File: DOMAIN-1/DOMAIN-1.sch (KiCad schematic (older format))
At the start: 245 parts, among them J1 Conn_02x10_Odd_Even, J2 AVR-ISP-6, SW1 SW_Push, U1 AT90USB1286-AU, U2 PRTR5V0U2X, Y1 Crystal_GND24_Small

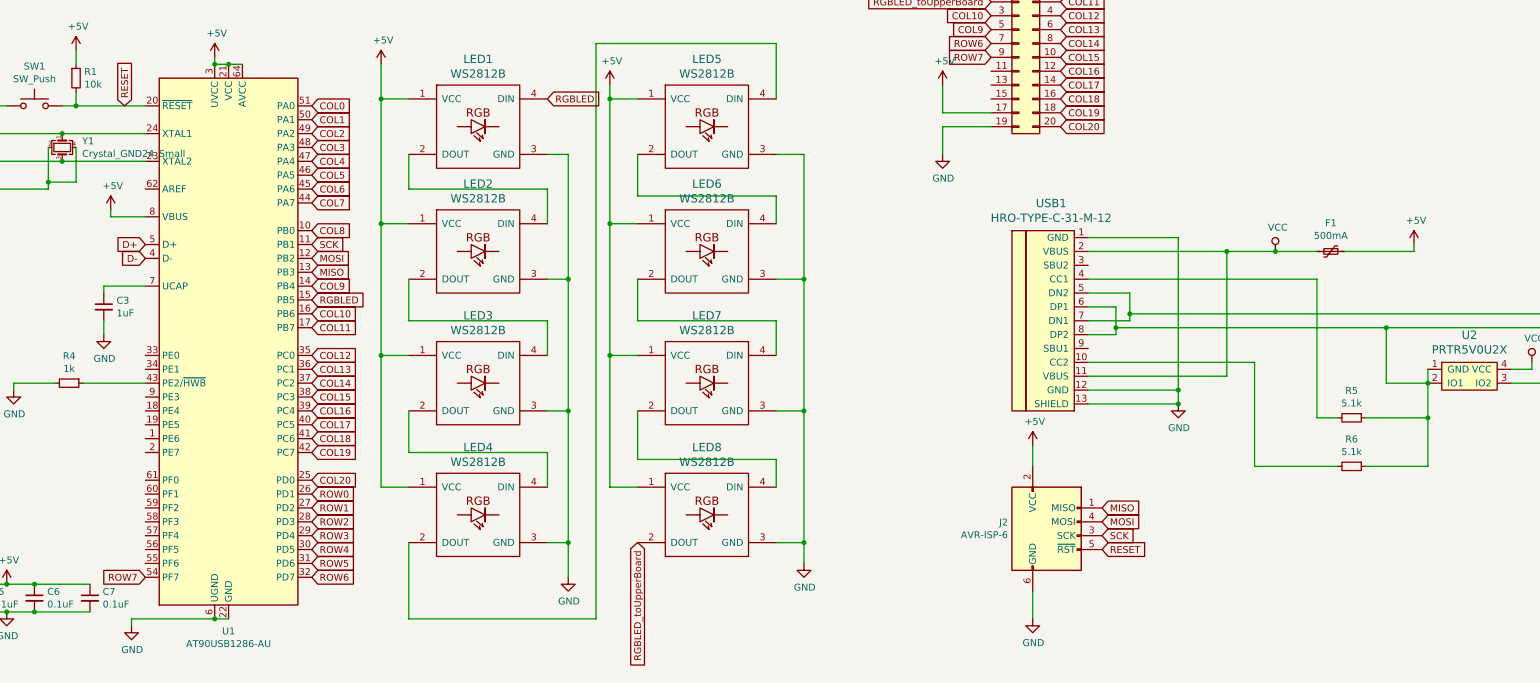
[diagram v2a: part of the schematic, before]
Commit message: Finished LED placement
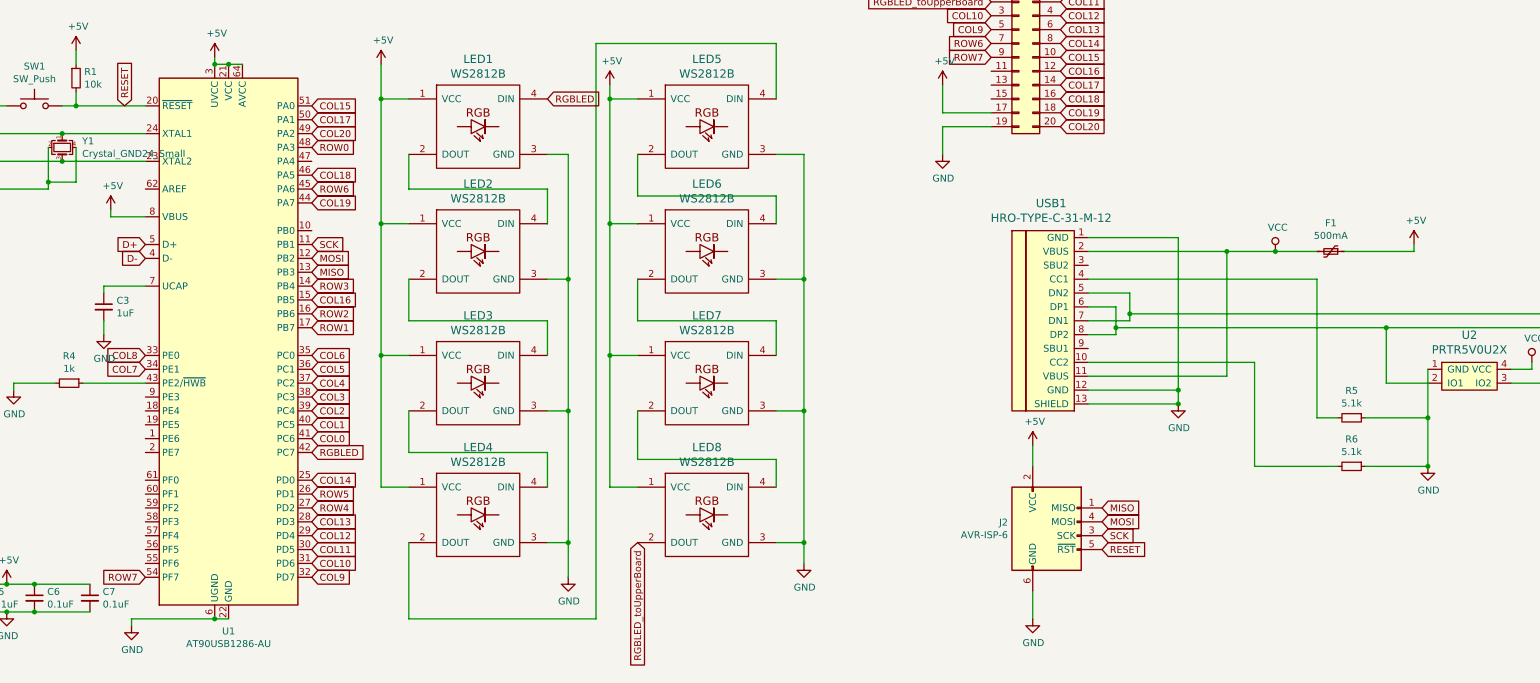
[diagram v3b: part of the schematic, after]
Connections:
- net COL0: now also U1.41 (PC6); no longer U1.51 (PA0)
- net COL1: now also U1.40 (PC5); no longer U1.50 (PA1)
- net COL10: now also U1.31 (PD6); no longer U1.16 (PB6)
- net COL11: now also U1.30 (PD5); no longer U1.17 (PB7)
- net COL12: now also U1.29 (PD4); no longer U1.35 (PC0)
- net COL13: now also U1.28 (PD3); no longer U1.36 (PC1)
- net COL14: now also U1.25 (PD0); no longer U1.37 (PC2)
- net COL15: now also U1.51 (PA0); no longer U1.38 (PC3)
- net COL16: now also U1.15 (PB5); no longer U1.39 (PC4)
- net COL17: now also U1.50 (PA1); no longer U1.40 (PC5)
- net COL18: now also U1.46 (PA5); no longer U1.41 (PC6)
- net COL19: now also U1.44 (PA7); no longer U1.42 (PC7)
- net COL2: now also U1.39 (PC4); no longer U1.49 (PA2)
- net COL20: now also U1.49 (PA2); no longer U1.25 (PD0)
- net COL3: now also U1.38 (PC3); no longer U1.48 (PA3)
- net COL4: now also U1.37 (PC2); no longer U1.47 (PA4)
- net COL5: now also U1.36 (PC1); no longer U1.46 (PA5)
- net COL6: now also U1.35 (PC0); no longer U1.45 (PA6)
- net COL7: now also U1.34 (PE1); no longer U1.44 (PA7)
- net COL8: now also U1.33 (PE0); no longer U1.10 (PB0)
- net COL9: now also U1.32 (PD7); no longer U1.14 (PB4)
- net GND: now also R5.1, R6.1, U2.1 (GND)
- net RGBLED: now also U1.42 (PC7); no longer U1.15 (PB5)
- net ROW0: now also U1.48 (PA3); no longer U1.26 (PD1)
- net ROW1: now also U1.17 (PB7); no longer U1.27 (PD2)
- net ROW2: now also U1.16 (PB6); no longer U1.28 (PD3)
- net ROW3: now also U1.14 (PB4); no longer U1.29 (PD4)
- net ROW4: now also U1.27 (PD2); no longer U1.30 (PD5)
- net ROW5: now also U1.26 (PD1); no longer U1.31 (PD6)
- net ROW6: now also U1.45 (PA6); no longer U1.32 (PD7)
- net at R3.2, U2.2 (IO1), USB1.6 (DP1)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: no longer R5.1, R6.1, U2.1 (GND)
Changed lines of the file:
@@
 Wire Wire Line
 	11500 9750 11050 9750
-Connection ~ 11500 9400
 Wire Wire Line
 	10700 8400 9050 8400
@@
 Wire Wire Line
 	11500 9400 11050 9400
-Wire Wire Line
-	11500 9150 11500 9400
-Connection ~ 11500 9150
-Wire Wire Line
-	11500 9050 11500 9150
 $Comp
 L power:VCC #PWR0103
@@
 Wire Wire Line
 	12100 9150 12350 9150
-$Comp
-L random-keyboard-parts:PRTR5V0U2X U2
-U 1 1 61D145CB
-P 11800 9100
-F 0 "U2" H 11800 9397 60  0000 C CNN
-F 1 "PRTR5V0U2X" H 11800 9291 60  0000 C CNN
-F 2 "random-keyboard-parts:SOT143B" H 11800 9100 60  0001 C CNN
-F 3 "" H 11800 9100 60  0001 C CNN
-	1    11800 9100
-	1    0    0    -1
-$EndComp
 Text GLabel 13150 8650 2    50   Input ~ 0
 D-
@@
 F 3 "~" H 1450 7350 50  0001 C CNN
 	1    1450 7150
-	1    0    0    -1
-$EndComp
-$Comp
-L MCU_Microchip_AVR:AT90USB1286-AU U1
-U 1 1 61D51A8D
-P 2850 8850
-F 0 "U1" H 2850 6761 50  0000 C CNN
-F 1 "AT90USB1286-AU" H 2850 6670 50  0000 C CNN
-F 2 "Package_QFP:TQFP-64_14x14mm_P0.8mm" H 2850 8850 50  0001 C CIN
-F 3 "http://ww1.microchip.com/downloads/en/DeviceDoc/doc7593.pdf" H 2850 8850 50  0001 C CNN
-	1    2850 8850
 	1    0    0    -1
 $EndComp
@@
 Text GLabel 5150 7100 2    50   Input ~ 0
 RGBLED
+Text GLabel 3450 9450 2    50   Input ~ 0
+COL1
+Text GLabel 3450 9250 2    50   Input ~ 0
+COL3
+Text GLabel 3450 9150 2    50   Input ~ 0
+COL4
+Text GLabel 3450 9050 2    50   Input ~ 0
+COL5
+Text GLabel 3450 8950 2    50   Input ~ 0
+COL6
+Text GLabel 3450 9550 2    50   Input ~ 0
+COL0
+Text GLabel 2250 9050 0    50   Input ~ 0
+COL7
+Text GLabel 2250 8950 0    50   Input ~ 0
+COL8
+Text GLabel 3450 10550 2    50   Input ~ 0
+COL9
+Text GLabel 3450 10450 2    50   Input ~ 0
+COL10
+Text GLabel 3450 10350 2    50   Input ~ 0
+COL11
+Text GLabel 3450 10250 2    50   Input ~ 0
+COL12
+Text GLabel 3450 10150 2    50   Input ~ 0
+COL13
+Text GLabel 3450 9850 2    50   Input ~ 0
+COL14
+Text GLabel 3450 7150 2    50   Input ~ 0
+COL15
+Text GLabel 3450 8550 2    50   Input ~ 0
+COL16
 Text GLabel 3450 7250 2    50   Input ~ 0
-COL1
+COL17
+Text GLabel 3450 7650 2    50   Input ~ 0
+COL18
+Text GLabel 3450 7850 2    50   Input ~ 0
+COL19
 Text GLabel 3450 7350 2    50   Input ~ 0
-COL2
+COL20
 Text GLabel 3450 7450 2    50   Input ~ 0
-COL3
-Text GLabel 3450 7550 2    50   Input ~ 0
-COL4
-Text GLabel 3450 7650 2    50   Input ~ 0
-COL5
-Text GLabel 3450 7750 2    50   Input ~ 0
-COL6
-Text GLabel 3450 7150 2    50   Input ~ 0
-COL0
-Text GLabel 3450 7850 2    50   Input ~ 0
-COL7
-Text GLabel 3450 8050 2    50   Input ~ 0
-COL8
+ROW0
+Text GLabel 3450 8750 2    50   Input ~ 0
+ROW1
+Text GLabel 3450 8650 2    50   Input ~ 0
+ROW2
 Text GLabel 3450 8450 2    50   Input ~ 0
-COL9
-Text GLabel 3450 8650 2    50   Input ~ 0
-COL10
-Text GLabel 3450 8750 2    50   Input ~ 0
-COL11
-Text GLabel 3450 8950 2    50   Input ~ 0
-COL12
-Text GLabel 3450 9050 2    50   Input ~ 0
-COL13
-Text GLabel 3450 9150 2    50   Input ~ 0
-COL14
-Text GLabel 3450 9250 2    50   Input ~ 0
-COL15
-Text GLabel 3450 9350 2    50   Input ~ 0
-COL16
-Text GLabel 3450 9450 2    50   Input ~ 0
-COL17
-Text GLabel 3450 9550 2    50   Input ~ 0
-COL18
-Text GLabel 3450 9650 2    50   Input ~ 0
-COL19
-Text GLabel 3450 9850 2    50   Input ~ 0
-COL20
+ROW3
 Text GLabel 3450 9950 2    50   Input ~ 0
-ROW0
-Text GLabel 3450 10050 2    50   Input ~ 0
-ROW1
-Text GLabel 3450 10150 2    50   Input ~ 0
-ROW2
-Text GLabel 3450 10250 2    50   Input ~ 0
-ROW3
-Text GLabel 3450 10350 2    50   Input ~ 0
-ROW4
-Text GLabel 3450 10450 2    50   Input ~ 0
 ROW5
 Text GLabel 3450 8150 2    50   Input ~ 0
@@
 Text GLabel 3450 8350 2    50   Input ~ 0
 MISO
-Text GLabel 3450 8550 2    50   Input ~ 0
+Text GLabel 3450 9650 2    50   Input ~ 0
 RGBLED
 $Comp
@@
 Text GLabel 5800 10300 3    50   Input ~ 0
 RGBLED_toUpperBoard
-Text GLabel 3450 10550 2    50   Input ~ 0
+Text GLabel 3450 7750 2    50   Input ~ 0
 ROW6
 Text GLabel 2250 10550 0    50   Input ~ 0
@@
 	1    0    0    -1
 $EndComp
+$Comp
+L power:GND #PWR0125
+U 1 1 62515AF3
+P 11500 9750
+F 0 "#PWR0125" H 11500 9500 50  0001 C CNN
+F 1 "GND" H 11505 9577 50  0000 C CNN
+F 2 "" H 11500 9750 50  0001 C CNN
+F 3 "" H 11500 9750 50  0001 C CNN
+	1    11500 9750
+	1    0    0    -1
+$EndComp
+Connection ~ 11500 9750
+$Comp
+L random-keyboard-parts:PRTR5V0U2X U2
+U 1 1 61D145CB
+P 11800 9100
+F 0 "U2" H 11800 9397 60  0000 C CNN
+F 1 "PRTR5V0U2X" H 11800 9291 60  0000 C CNN
+F 2 "random-keyboard-parts:SOT143B" H 11800 9100 60  0001 C CNN
+F 3 "" H 11800 9100 60  0001 C CNN
+	1    11800 9100
+	1    0    0    -1
+$EndComp
+Connection ~ 11500 9400
+Wire Wire Line
+	11500 9050 11500 9400
+$Comp
+L MCU_Microchip_AVR:AT90USB1286-AU U1
+U 1 1 61D51A8D
+P 2850 8850
+F 0 "U1" H 2850 6761 50  0000 C CNN
+F 1 "AT90USB1286-AU" H 2850 6670 50  0000 C CNN
+F 2 "Package_QFP:TQFP-64_14x14mm_P0.8mm" H 2850 8850 50  0001 C CIN
+F 3 "http://ww1.microchip.com/downloads/en/DeviceDoc/doc7593.pdf" H 2850 8850 50  0001 C CNN
+	1    2850 8850
+	1    0    0    -1
+$EndComp
+Text GLabel 3450 9350 2    50   Input ~ 0
+COL2
+Text GLabel 3450 10050 2    50   Input ~ 0
+ROW4
 $EndSCHEMATC

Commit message: Finished mainboard
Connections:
- net +5V: now also J1.1 (Pin_1); no longer J1.17 (Pin_17)
- net COL10: now also J1.16 (Pin_16); no longer J1.3 (Pin_3)
- net COL11: now also J1.4 (Pin_4); no longer J1.2 (Pin_2)
- net COL12: now also J1.6 (Pin_6); no longer J1.4 (Pin_4)
- net COL13: now also J1.8 (Pin_8); no longer J1.6 (Pin_6)
- net COL14: now also J1.10 (Pin_10); no longer J1.8 (Pin_8)
- net COL15: now also J1.12 (Pin_12), U1.57 (PF4); no longer J1.10 (Pin_10), U1.51 (PA0)
- net COL16: now also J1.14 (Pin_14), U1.56 (PF5); no longer J1.12 (Pin_12), U1.15 (PB5)
- net COL17: now also J1.9 (Pin_9), U1.18 (PE4); no longer J1.14 (Pin_14), U1.50 (PA1)
- net COL18: now also J1.7 (Pin_7), U1.17 (PB7); no longer J1.16 (Pin_16), U1.46 (PA5)
- net COL19: now also J1.5 (Pin_5), U1.16 (PB6); no longer J1.18 (Pin_18), U1.44 (PA7)
- net COL20: now also J1.3 (Pin_3), U1.15 (PB5); no longer J1.20 (Pin_20), U1.49 (PA2)
- net COL9: now also J1.20 (Pin_20); no longer J1.5 (Pin_5)
- net RGBLED_toUpperBoard: now also J1.2 (Pin_2); no longer J1.1 (Pin_1)
- net ROW0: now also U1.58 (PF3); no longer U1.48 (PA3)
- net ROW1: now also U1.55 (PF6); no longer U1.17 (PB7)
- net ROW2: now also U1.54 (PF7); no longer U1.16 (PB6)
- net ROW3: now also U1.19 (PE5); no longer U1.14 (PB4)
- net ROW6: now also J1.13 (Pin_13), U1.14 (PB4); no longer J1.7 (Pin_7), U1.45 (PA6)
- net ROW7: now also J1.15 (Pin_15), U1.10 (PB0); no longer J1.9 (Pin_9), U1.54 (PF7)
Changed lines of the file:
@@
 Text GLabel 3450 9850 2    50   Input ~ 0
 COL14
-Text GLabel 3450 7150 2    50   Input ~ 0
-COL15
+Text GLabel 2250 10350 0    50   Input ~ 0
+COL16
+Text GLabel 2250 9350 0    50   Input ~ 0
+COL17
+Text GLabel 3450 8750 2    50   Input ~ 0
+COL18
+Text GLabel 3450 8650 2    50   Input ~ 0
+COL19
 Text GLabel 3450 8550 2    50   Input ~ 0
-COL16
-Text GLabel 3450 7250 2    50   Input ~ 0
-COL17
-Text GLabel 3450 7650 2    50   Input ~ 0
-COL18
-Text GLabel 3450 7850 2    50   Input ~ 0
-COL19
-Text GLabel 3450 7350 2    50   Input ~ 0
 COL20
-Text GLabel 3450 7450 2    50   Input ~ 0
+Text GLabel 2250 10150 0    50   Input ~ 0
 ROW0
-Text GLabel 3450 8750 2    50   Input ~ 0
+Text GLabel 2250 10450 0    50   Input ~ 0
 ROW1
-Text GLabel 3450 8650 2    50   Input ~ 0
+Text GLabel 2250 10550 0    50   Input ~ 0
 ROW2
-Text GLabel 3450 8450 2    50   Input ~ 0
+Text GLabel 2250 9450 0    50   Input ~ 0
 ROW3
 Text GLabel 3450 9950 2    50   Input ~ 0
@@
 	1    0    0    -1
 $EndComp
+Text GLabel 8350 6500 0    50   Input ~ 0
+COL20
+Text GLabel 8350 6600 0    50   Input ~ 0
+COL19
+Text GLabel 8350 6700 0    50   Input ~ 0
+COL18
+Text GLabel 8350 6800 0    50   Input ~ 0
+COL17
+Text GLabel 8850 7000 2    50   Input ~ 0
+COL16
+Text GLabel 8850 6900 2    50   Input ~ 0
+COL15
+Text GLabel 8850 6800 2    50   Input ~ 0
+COL14
+Text GLabel 8850 6700 2    50   Input ~ 0
+COL13
+Text GLabel 8850 6600 2    50   Input ~ 0
+COL12
+Text GLabel 8850 6500 2    50   Input ~ 0
+COL11
+Text GLabel 8850 6400 2    50   Input ~ 0
+RGBLED_toUpperBoard
+Text GLabel 8850 7100 2    50   Input ~ 0
+COL10
 Text GLabel 8850 7300 2    50   Input ~ 0
-COL20
-Text GLabel 8850 7200 2    50   Input ~ 0
-COL19
-Text GLabel 8850 7100 2    50   Input ~ 0
-COL18
-Text GLabel 8850 7000 2    50   Input ~ 0
-COL17
-Text GLabel 8850 6900 2    50   Input ~ 0
-COL16
-Text GLabel 8850 6800 2    50   Input ~ 0
-COL15
-Text GLabel 8850 6700 2    50   Input ~ 0
-COL14
-Text GLabel 8850 6600 2    50   Input ~ 0
-COL13
-Text GLabel 8850 6500 2    50   Input ~ 0
-COL12
-Text GLabel 8850 6400 2    50   Input ~ 0
-COL11
-Text GLabel 8350 6400 0    50   Input ~ 0
-RGBLED_toUpperBoard
-Text GLabel 8350 6500 0    50   Input ~ 0
-COL10
-Text GLabel 8350 6600 0    50   Input ~ 0
 COL9
-Text GLabel 8350 6700 0    50   Input ~ 0
+Text GLabel 8350 7000 0    50   Input ~ 0
 ROW6
-Text GLabel 8350 6800 0    50   Input ~ 0
+Text GLabel 8350 7100 0    50   Input ~ 0
 ROW7
 Wire Wire Line
-	8350 7200 8000 7200
-Wire Wire Line
-	8000 7200 8000 7000
+	8350 6400 8000 6400
+Wire Wire Line
+	8000 6400 8000 6200
 Wire Wire Line
 	8350 7300 8000 7300
@@
 L power:+5V #PWR0121
 U 1 1 61EEE90C
-P 8000 7000
-F 0 "#PWR0121" H 8000 6850 50  0001 C CNN
-F 1 "+5V" H 8015 7173 50  0000 C CNN
-F 2 "" H 8000 7000 50  0001 C CNN
-F 3 "" H 8000 7000 50  0001 C CNN
-	1    8000 7000
+P 8000 6200
+F 0 "#PWR0121" H 8000 6050 50  0001 C CNN
+F 1 "+5V" H 8015 6373 50  0000 C CNN
+F 2 "" H 8000 6200 50  0001 C CNN
+F 3 "" H 8000 6200 50  0001 C CNN
+	1    8000 6200
 	1    0    0    -1
 $EndComp
@@
 Text GLabel 5800 10300 3    50   Input ~ 0
 RGBLED_toUpperBoard
-Text GLabel 3450 7750 2    50   Input ~ 0
-ROW6
-Text GLabel 2250 10550 0    50   Input ~ 0
-ROW7
 $Comp
 L Device:C_Small C8
@@
 Text GLabel 3450 10050 2    50   Input ~ 0
 ROW4
+Text GLabel 3450 8050 2    50   Input ~ 0
+ROW7
+Text GLabel 3450 8450 2    50   Input ~ 0
+ROW6
+Text GLabel 2250 10250 0    50   Input ~ 0
+COL15
 $EndSCHEMATC
